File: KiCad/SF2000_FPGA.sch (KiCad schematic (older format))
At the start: 18 parts, among them J10 Conn_02x01, J11 Conn_02x01, J12 Conn_01x01, J3 Conn_02x03_Odd_Even, J4 Conn_02x01, J8 Conn_02x01, J9 Conn_02x01, U3 74LVC2G14, U7 10M04SCE144

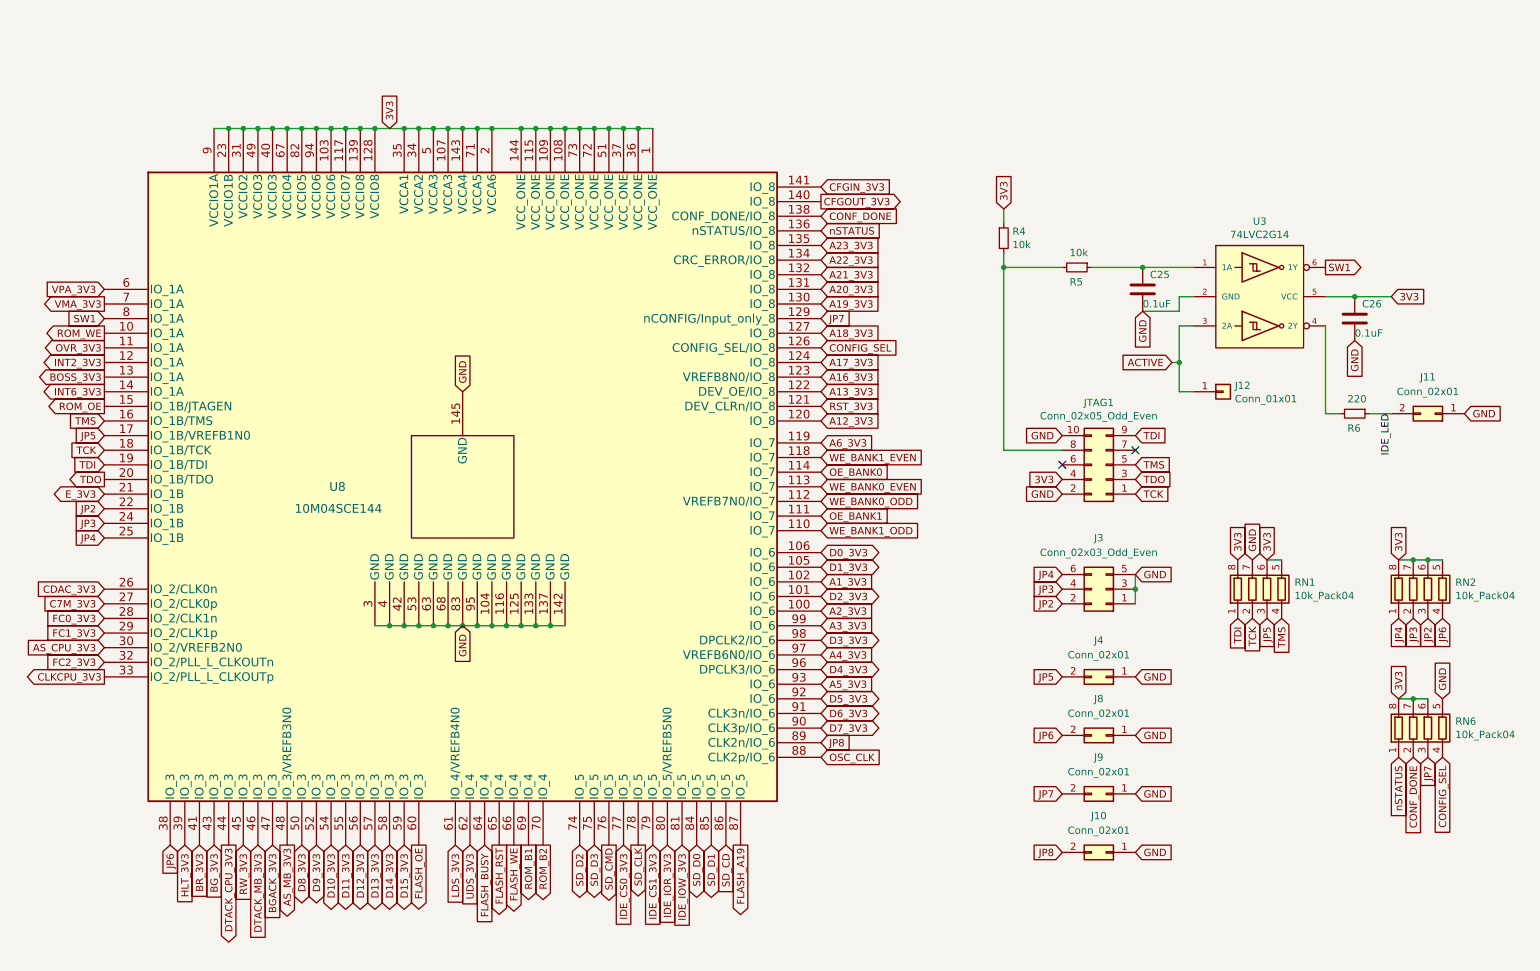
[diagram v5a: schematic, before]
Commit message: removed INT6_3V3 signal to FPGA and put in JP9 with a pull-up resistor instead
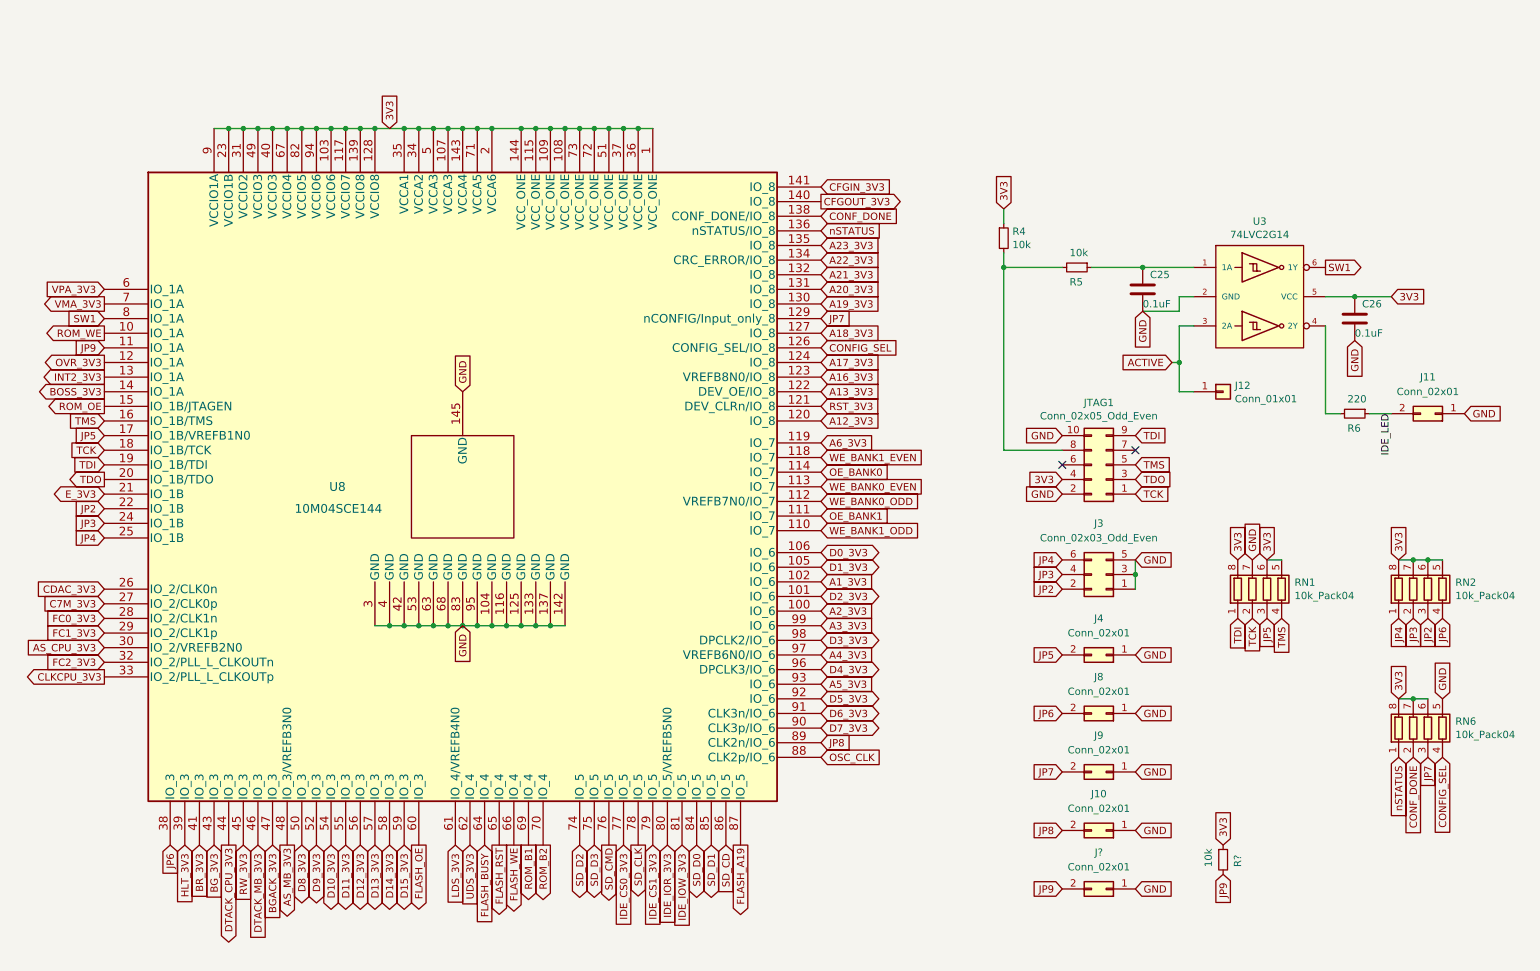
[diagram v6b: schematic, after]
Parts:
- added J?: Conn_02x01, Connector_PinHeader_2.00mm:PinHeader_2x01_P2.00mm_Vertical, symbol Connector_Generic:Conn_02x01
- added R?: 10k, Resistor_SMD:R_0805_2012Metric_Pad1.15x1.40mm_HandSolder, symbol Device:R_Small
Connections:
- net INT6_3V3 is gone; now on net BOSS_3V3: U7.14 (IO_1A)
- net 3V3: now also R?.1
- net BOSS_3V3: no longer U7.13 (IO_1A)
- net GND: now also J?.1 (Pin_1)
- net INT2_3V3: now also U7.13 (IO_1A); no longer U7.12 (IO_1A)
- net OVR_3V3: now also U7.12 (IO_1A); no longer U7.11 (IO_1A)
- new net JP9: J?.2 (Pin_2), R?.2, U7.11 (IO_1A)
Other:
- moved on the sheet: J10, J3, J4, J8, J9
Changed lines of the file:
@@
 Text GLabel 1350 2500 0    50   Output ~ 0
 ROM_WE
-Text GLabel 1350 2600 0    50   Output ~ 0
+Text GLabel 1350 2700 0    50   Output ~ 0
 OVR_3V3
-Text GLabel 1350 2700 0    50   Output ~ 0
+Text GLabel 1350 2800 0    50   Output ~ 0
 INT2_3V3
 Wire Wire Line
@@
 Text GLabel 3300 1100 1    50   Input ~ 0
 3V3
-Text GLabel 1350 2800 0    50   Output ~ 0
+Text GLabel 1350 2900 0    50   Output ~ 0
 BOSS_3V3
-Text GLabel 1350 2900 0    50   Output ~ 0
-INT6_3V3
 Text GLabel 1350 4450 0    50   Input ~ 0
 FC0_3V3
@@
 Text GLabel 1350 2400 0    50   Input ~ 0
 SW1
-Text GLabel 7900 4850 0    50   Input ~ 0
+Text GLabel 7900 4700 0    50   Input ~ 0
 JP5
 $Comp
@@
 L Connector_Generic:Conn_02x03_Odd_Even J3
 U 1 1 62704BD7
-P 8200 4250
-F 0 "J3" H 8250 3900 50  0000 C CNN
-F 1 "Conn_02x03_Odd_Even" H 8250 4000 50  0000 C CNN
-F 2 "Connector_PinHeader_2.00mm:PinHeader_2x03_P2.00mm_Vertical" H 8200 4250 50  0001 C CNN
-F 3 "~" H 8200 4250 50  0001 C CNN
-	1    8200 4250
-	-1   0    0    1
-$EndComp
+P 8200 4150
+F 0 "J3" H 8250 3800 50  0000 C CNN
+F 1 "Conn_02x03_Odd_Even" H 8250 3900 50  0000 C CNN
+F 2 "Connector_PinHeader_2.00mm:PinHeader_2x03_P2.00mm_Vertical" H 8200 4150 50  0001 C CNN
+F 3 "~" H 8200 4150 50  0001 C CNN
+	1    8200 4150
+	-1   0    0    1
+$EndComp
+Text GLabel 7900 4150 0    50   Input ~ 0
+JP3
 Text GLabel 7900 4250 0    50   Input ~ 0
-JP3
-Text GLabel 7900 4350 0    50   Input ~ 0
 JP2
-Text GLabel 7900 4150 0    50   Input ~ 0
+Text GLabel 7900 4050 0    50   Input ~ 0
 JP4
 Wire Wire Line
+	8400 4050 8400 4150
+Connection ~ 8400 4150
+Wire Wire Line
 	8400 4150 8400 4250
-Connection ~ 8400 4250
-Wire Wire Line
-	8400 4250 8400 4350
-Text GLabel 8400 4150 2    50   Input ~ 0
+Text GLabel 8400 4050 2    50   Input ~ 0
 GND
 Text GLabel 1350 3800 0    50   Input ~ 0
@@
 L Connector_Generic:Conn_02x01 J4
 U 1 1 6276C760
-P 8200 4850
-F 0 "J4" H 8250 4600 50  0000 C CNN
-F 1 "Conn_02x01" H 8250 4700 50  0000 C CNN
-F 2 "Connector_PinHeader_2.00mm:PinHeader_2x01_P2.00mm_Vertical" H 8200 4850 50  0001 C CNN
-F 3 "~" H 8200 4850 50  0001 C CNN
-	1    8200 4850
-	-1   0    0    1
-$EndComp
-Text GLabel 8400 4850 2    50   Input ~ 0
+P 8200 4700
+F 0 "J4" H 8250 4450 50  0000 C CNN
+F 1 "Conn_02x01" H 8250 4550 50  0000 C CNN
+F 2 "Connector_PinHeader_2.00mm:PinHeader_2x01_P2.00mm_Vertical" H 8200 4700 50  0001 C CNN
+F 3 "~" H 8200 4700 50  0001 C CNN
+	1    8200 4700
+	-1   0    0    1
+$EndComp
+Text GLabel 8400 4700 2    50   Input ~ 0
 GND
 Text GLabel 9700 2050 2    50   Output ~ 0
@@
 L Connector_Generic:Conn_02x01 J9
 U 1 1 62127717
-P 8200 5650
-F 0 "J9" H 8250 5400 50  0000 C CNN
-F 1 "Conn_02x01" H 8250 5500 50  0000 C CNN
-F 2 "Connector_PinHeader_2.00mm:PinHeader_2x01_P2.00mm_Vertical" H 8200 5650 50  0001 C CNN
-F 3 "~" H 8200 5650 50  0001 C CNN
-	1    8200 5650
-	-1   0    0    1
-$EndComp
-Text GLabel 8400 5650 2    50   Input ~ 0
-GND
-Text GLabel 7900 5650 0    50   Input ~ 0
+P 8200 5500
+F 0 "J9" H 8250 5250 50  0000 C CNN
+F 1 "Conn_02x01" H 8250 5350 50  0000 C CNN
+F 2 "Connector_PinHeader_2.00mm:PinHeader_2x01_P2.00mm_Vertical" H 8200 5500 50  0001 C CNN
+F 3 "~" H 8200 5500 50  0001 C CNN
+	1    8200 5500
+	-1   0    0    1
+$EndComp
+Text GLabel 8400 5500 2    50   Input ~ 0
+GND
+Text GLabel 7900 5500 0    50   Input ~ 0
 JP7
 $Comp
 L Connector_Generic:Conn_02x01 J10
 U 1 1 62132436
-P 8200 6050
-F 0 "J10" H 8250 5800 50  0000 C CNN
-F 1 "Conn_02x01" H 8250 5900 50  0000 C CNN
-F 2 "Connector_PinHeader_2.00mm:PinHeader_2x01_P2.00mm_Vertical" H 8200 6050 50  0001 C CNN
-F 3 "~" H 8200 6050 50  0001 C CNN
-	1    8200 6050
-	-1   0    0    1
-$EndComp
-Text GLabel 8400 6050 2    50   Input ~ 0
-GND
-Text GLabel 7900 6050 0    50   Input ~ 0
+P 8200 5900
+F 0 "J10" H 8250 5650 50  0000 C CNN
+F 1 "Conn_02x01" H 8250 5750 50  0000 C CNN
+F 2 "Connector_PinHeader_2.00mm:PinHeader_2x01_P2.00mm_Vertical" H 8200 5900 50  0001 C CNN
+F 3 "~" H 8200 5900 50  0001 C CNN
+	1    8200 5900
+	-1   0    0    1
+$EndComp
+Text GLabel 8400 5900 2    50   Input ~ 0
+GND
+Text GLabel 7900 5900 0    50   Input ~ 0
 JP8
 Text GLabel 6250 5300 2    50   Input ~ 0
@@
 Text GLabel 10400 5400 3    50   Input ~ 0
 JP7
-Text GLabel 7900 5250 0    50   Input ~ 0
+Text GLabel 7900 5100 0    50   Input ~ 0
 JP6
 $Comp
 L Connector_Generic:Conn_02x01 J8
 U 1 1 621772F2
-P 8200 5250
-F 0 "J8" H 8250 5000 50  0000 C CNN
-F 1 "Conn_02x01" H 8250 5100 50  0000 C CNN
-F 2 "Connector_PinHeader_2.00mm:PinHeader_2x01_P2.00mm_Vertical" H 8200 5250 50  0001 C CNN
-F 3 "~" H 8200 5250 50  0001 C CNN
-	1    8200 5250
-	-1   0    0    1
-$EndComp
-Text GLabel 8400 5250 2    50   Input ~ 0
+P 8200 5100
+F 0 "J8" H 8250 4850 50  0000 C CNN
+F 1 "Conn_02x01" H 8250 4950 50  0000 C CNN
+F 2 "Connector_PinHeader_2.00mm:PinHeader_2x01_P2.00mm_Vertical" H 8200 5100 50  0001 C CNN
+F 3 "~" H 8200 5100 50  0001 C CNN
+	1    8200 5100
+	-1   0    0    1
+$EndComp
+Text GLabel 8400 5100 2    50   Input ~ 0
 GND
 Text GLabel 10500 4450 3    50   Input ~ 0
@@
 	8700 2900 8800 2900
 Connection ~ 8700 2700
+$Comp
+L Connector_Generic:Conn_02x01 J?
+U 1 1 6268BA13
+P 8200 6300
+F 0 "J?" H 8250 6050 50  0000 C CNN
+F 1 "Conn_02x01" H 8250 6150 50  0000 C CNN
+F 2 "Connector_PinHeader_2.00mm:PinHeader_2x01_P2.00mm_Vertical" H 8200 6300 50  0001 C CNN
+F 3 "~" H 8200 6300 50  0001 C CNN
+	1    8200 6300
+	-1   0    0    1
+$EndComp
+Text GLabel 8400 6300 2    50   Input ~ 0
+GND
+Text GLabel 7900 6300 0    50   Input ~ 0
+JP9
+Text GLabel 1350 2600 0    50   Input ~ 0
+JP9
+$Comp
+L Device:R_Small R?
+U 1 1 626987D6
+P 9000 6100
+AR Path="/626987D6" Ref="R?"  Part="1"
+AR Path="/620D263D/626987D6" Ref="R?"  Part="1"
+F 0 "R?" V 9100 6050 50  0000 L CNN
+F 1 "10k" V 8900 6050 50  0000 L CNN
+F 2 "Resistor_SMD:R_0805_2012Metric_Pad1.15x1.40mm_HandSolder" H 9000 6100 50  0001 C CNN
+F 3 "~" H 9000 6100 50  0001 C CNN
+	1    9000 6100
+	1    0    0    -1
+$EndComp
+Text GLabel 9000 6200 3    50   Input ~ 0
+JP9
+Text GLabel 9000 6000 1    50   Input ~ 0
+3V3
 $EndSCHEMATC

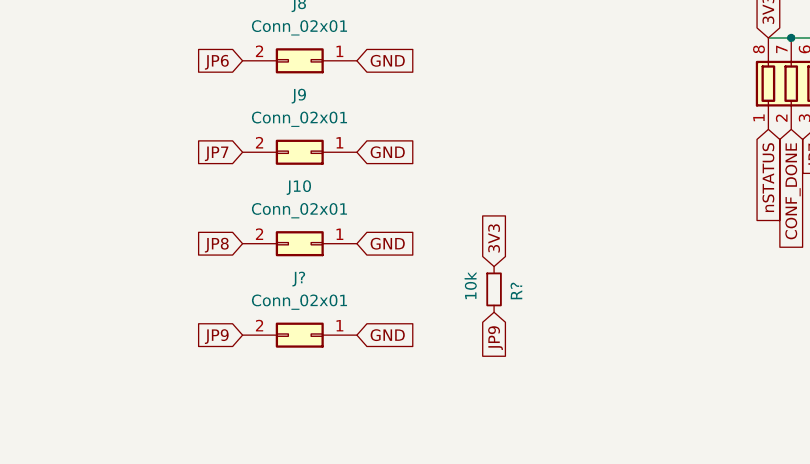
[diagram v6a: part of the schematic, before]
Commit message: added tables with Jumper-setting explanations on silkscreen
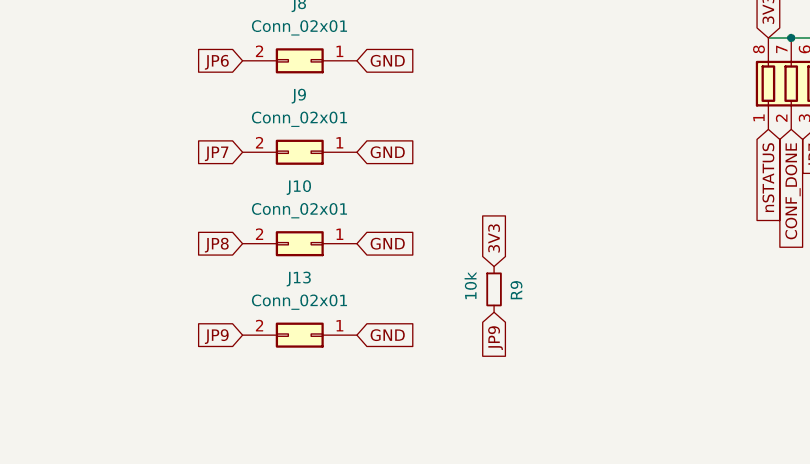
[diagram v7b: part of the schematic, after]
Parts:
- gave numbers to parts that had none: 2
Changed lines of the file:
@@
 Connection ~ 8700 2700
 $Comp
-L Connector_Generic:Conn_02x01 J?
+L Connector_Generic:Conn_02x01 J13
 U 1 1 6268BA13
 P 8200 6300
-F 0 "J?" H 8250 6050 50  0000 C CNN
+F 0 "J13" H 8250 6050 50  0000 C CNN
 F 1 "Conn_02x01" H 8250 6150 50  0000 C CNN
 F 2 "Connector_PinHeader_2.00mm:PinHeader_2x01_P2.00mm_Vertical" H 8200 6300 50  0001 C CNN
@@
 P 9000 6100
 AR Path="/626987D6" Ref="R?"  Part="1"
-AR Path="/620D263D/626987D6" Ref="R?"  Part="1"
-F 0 "R?" V 9100 6050 50  0000 L CNN
+AR Path="/620D263D/626987D6" Ref="R9"  Part="1"
+F 0 "R9" V 9100 6050 50  0000 L CNN
 F 1 "10k" V 8900 6050 50  0000 L CNN
 F 2 "Resistor_SMD:R_0805_2012Metric_Pad1.15x1.40mm_HandSolder" H 9000 6100 50  0001 C CNN
